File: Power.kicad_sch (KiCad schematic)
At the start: 26 parts, among them J8 USB_C_USB2.0_16P, Q1 Si2301CDS, Q2 Si2301CDS, U3 AMS1117-3.3, U4 TPS61230DRCR

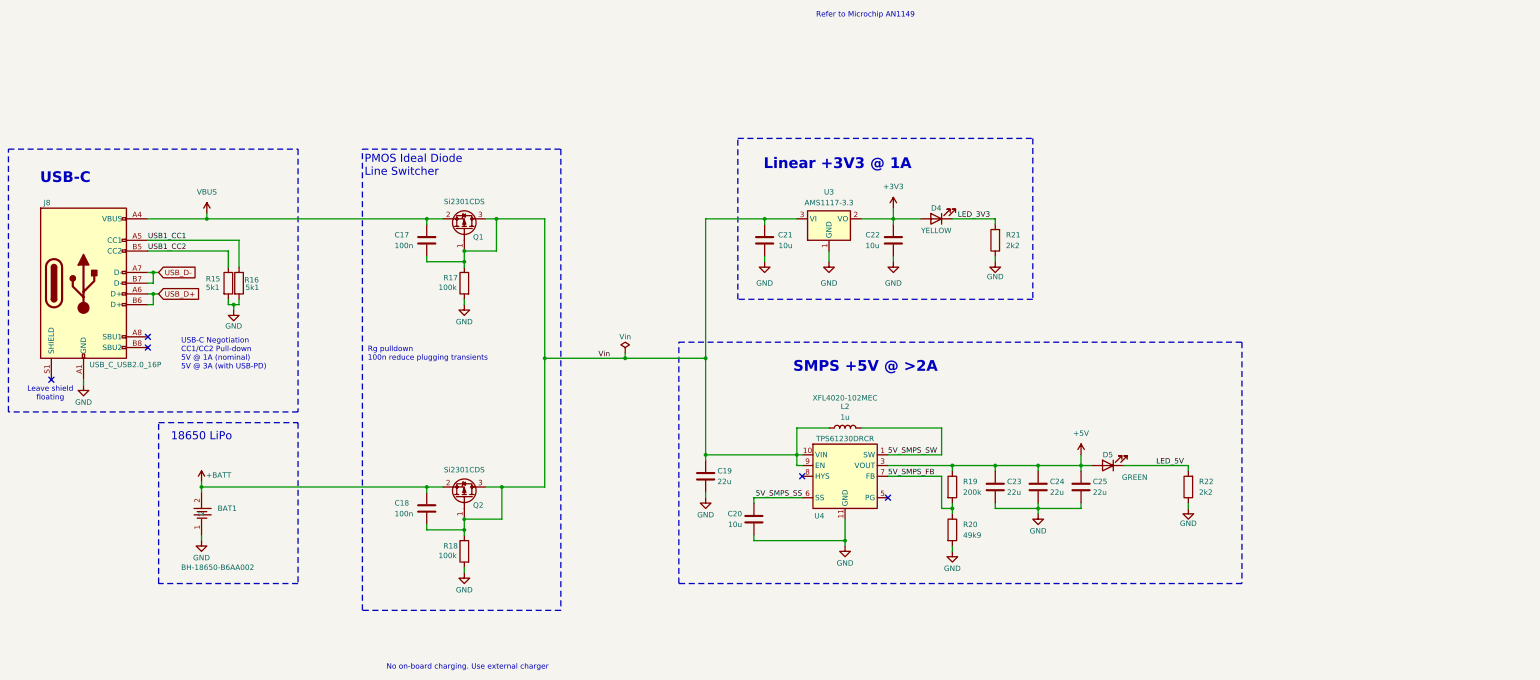
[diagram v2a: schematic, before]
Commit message: Add Buck-Boost 3V3 power
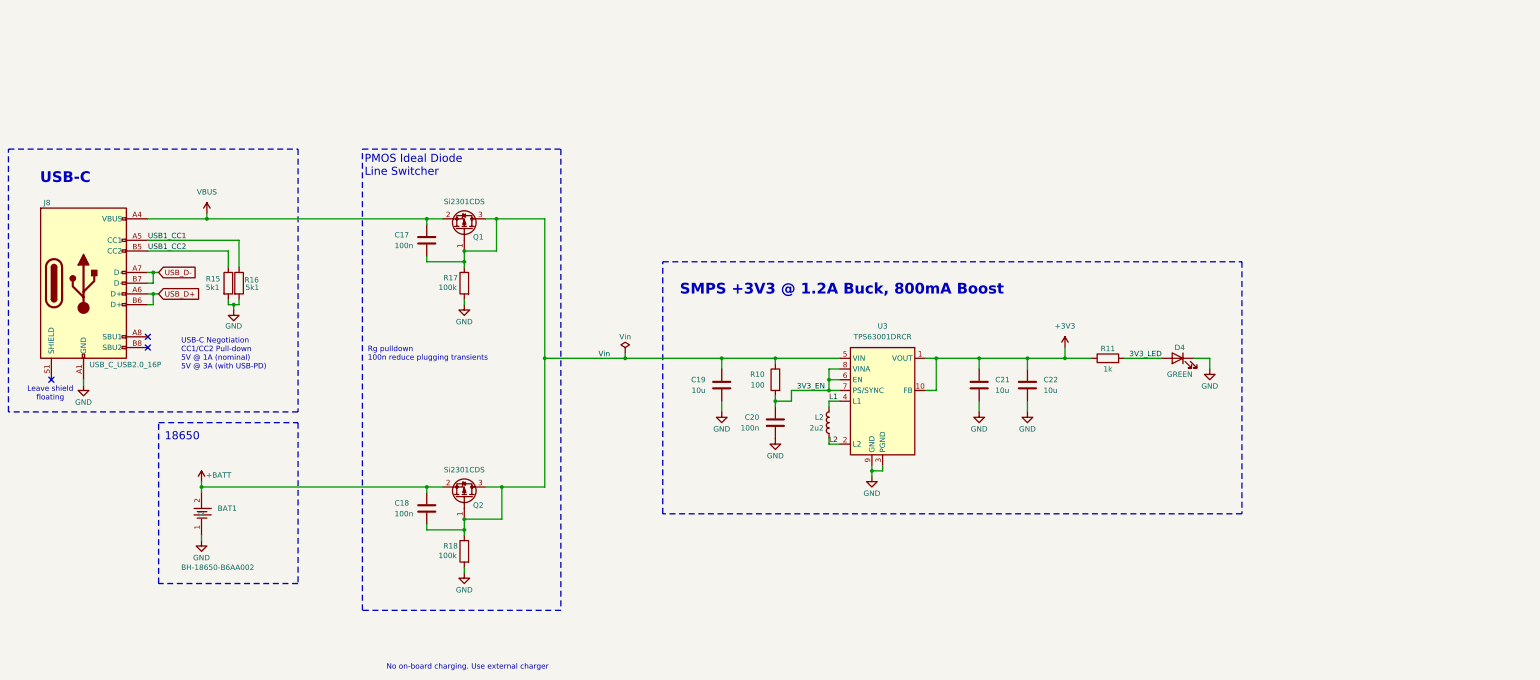
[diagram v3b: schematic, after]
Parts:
- removed C23, C24, C25: 22u, Capacitor_SMD:C_0805_2012Metric, symbol Device:C
- removed D5: GREEN, LED_SMD:LED_0603_1608Metric, symbol Device:LED
- removed R19: 200k, Resistor_SMD:R_0402_1005Metric, symbol Device:R
- removed R20: 49k9, Resistor_SMD:R_0402_1005Metric, symbol Device:R
- removed R21, R22: 2k2, Resistor_SMD:R_0603_1608Metric, symbol Device:R
- removed U3: AMS1117-3.3, Package_TO_SOT_SMD:SOT-223-3_TabPin2, symbol Regulator_Linear:AMS1117-3.3
- removed U4: TPS61230DRCR, Package_SON:Texas_S-PVSON-N10_ThermalVias, symbol Regulator_Switching:TPS61230DRC
- added R10: 100, Resistor_SMD:R_0402_1005Metric, symbol Device:R
- added R11: 1k, Resistor_SMD:R_0603_1608Metric, symbol Device:R
- added U3: TPS63001DRCR, Package_SON:Texas_DRC0010J_ThermalVias, symbol Regulator_Switching:TPS63001
- C19: value 22u -> 10u; footprint Capacitor_SMD:C_0805_2012Metric -> Capacitor_SMD:C_0603_1608Metric
- C20: value 10u -> 100n; footprint Capacitor_SMD:C_0603_1608Metric -> Capacitor_SMD:C_0402_1005Metric
- C21, C22: footprint Capacitor_SMD:C_0805_2012Metric -> Capacitor_SMD:C_0603_1608Metric
- D4: value YELLOW -> GREEN; footprint LED_SMD:LED_0603_1608Metric -> LED_SMD:LED_0805_2012Metric
- L2: value 1u -> 2u2; footprint easyeda2kicad:IND-SMD_L4.0-W4.0_XFL4020-102MEB -> easyeda2kicad:IND-SMD_L4.0-W4.0_VLS4012ET; LCSC Part C5355380 -> (none)
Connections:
- net LED_3V3 is gone; now on net GND: D4.1 (K)
- net +3V3: now also C21.1, R11.1, U3.1 (VOUT), U3.10 (FB); no longer D4.2 (A)
- net GND: now also U3.11 (PGND), U3.3 (PGND), U3.9 (GND)
- net Vin: now also R10.1, U3.5 (VIN); no longer C21.1, L2.1
- net 5V_SMPS_SS renamed 3V3_EN
- net 3V3_EN: now also R10.2, U3.6 (EN), U3.7 (PS/SYNC), U3.8 (VINA)
- net 5V_SMPS_SW renamed L2
- net L2: now also U3.2 (L2)
- new net 3V3_LED: D4.2 (A), R11.2
- new net L1: L2.1, U3.4 (L1)
- no-connect marks 5 -> 3
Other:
- note added: "18650"
- note added: "SMPS +3V3 @ 1.2A Buck, 800mA Boost"
- note removed: "18650 LiPo"
- note removed: "Linear +3V3 @ 1A"
- note removed: "Refer to Microchip AN1149"
- note removed: "SMPS +5V @ >2A"

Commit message: Added silkscreens label description and fixed DRC
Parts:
- U3: footprint Package_SON:Texas_DRC0010J_ThermalVias -> Package_SON:Texas_DRC0010J
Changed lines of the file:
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@@
 			)
 		)
-		(property "Footprint" "Package_SON:Texas_DRC0010J_ThermalVias"
+		(property "Footprint" "Package_SON:Texas_DRC0010J"
 			(at 261.62 120.65 0)
 			(effects

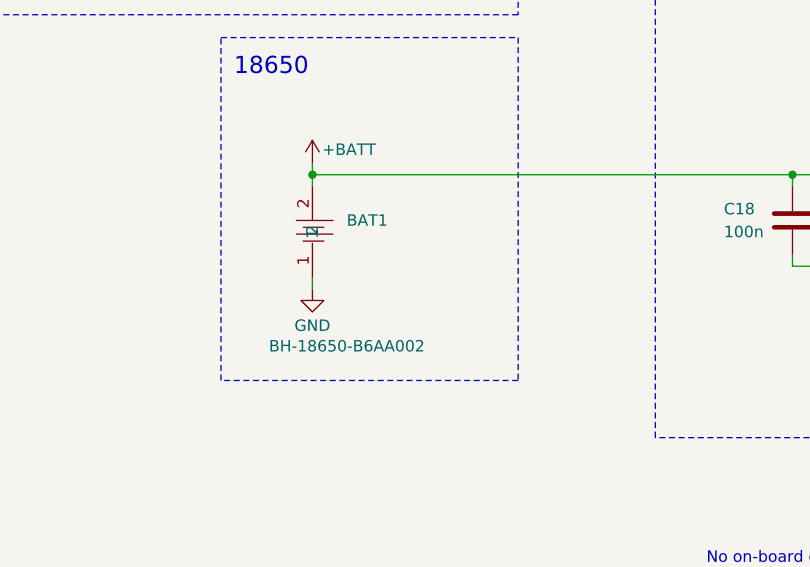
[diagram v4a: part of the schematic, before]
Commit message: Added 3D models and LCSC part numbers
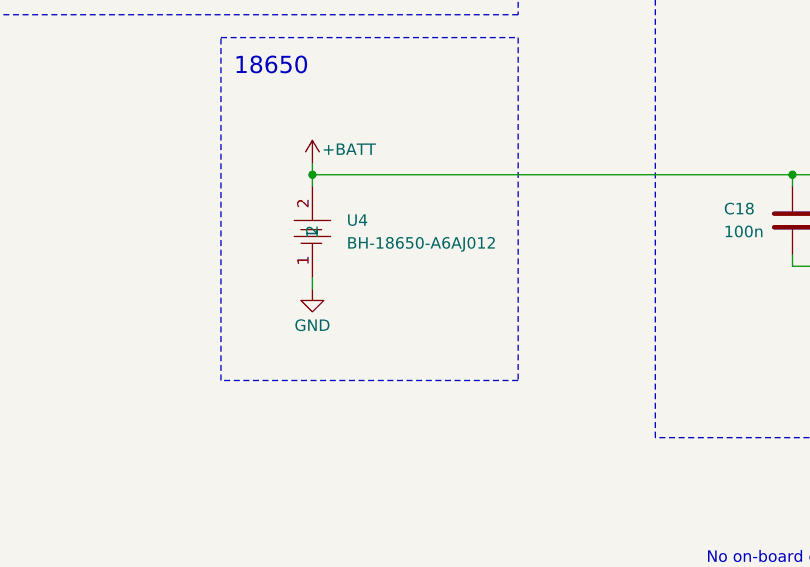
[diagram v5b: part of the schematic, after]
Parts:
- removed BAT1: BH-18650-B6AA002, easyeda2kicad:BATTERY-SMD_18650-1S-L77.1-W20.7-1, symbol easyeda2kicad:BH-18650-B6AA002
- added U4: BH-18650-A6AJ012, easyeda2kicad:BAT-TH_BH-18650-A6AJ012, symbol easyeda2kicad:BH-18650-A6AJ012
- J8: LCSC Part (none) -> C165948
- L2: LCSC Part (none) -> C76867
- Q1, Q2: LCSC Part (none) -> C10487
- U3: LCSC Part (none) -> C28060
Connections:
- net +BATT: now also U4.2
- net GND: now also U4.1

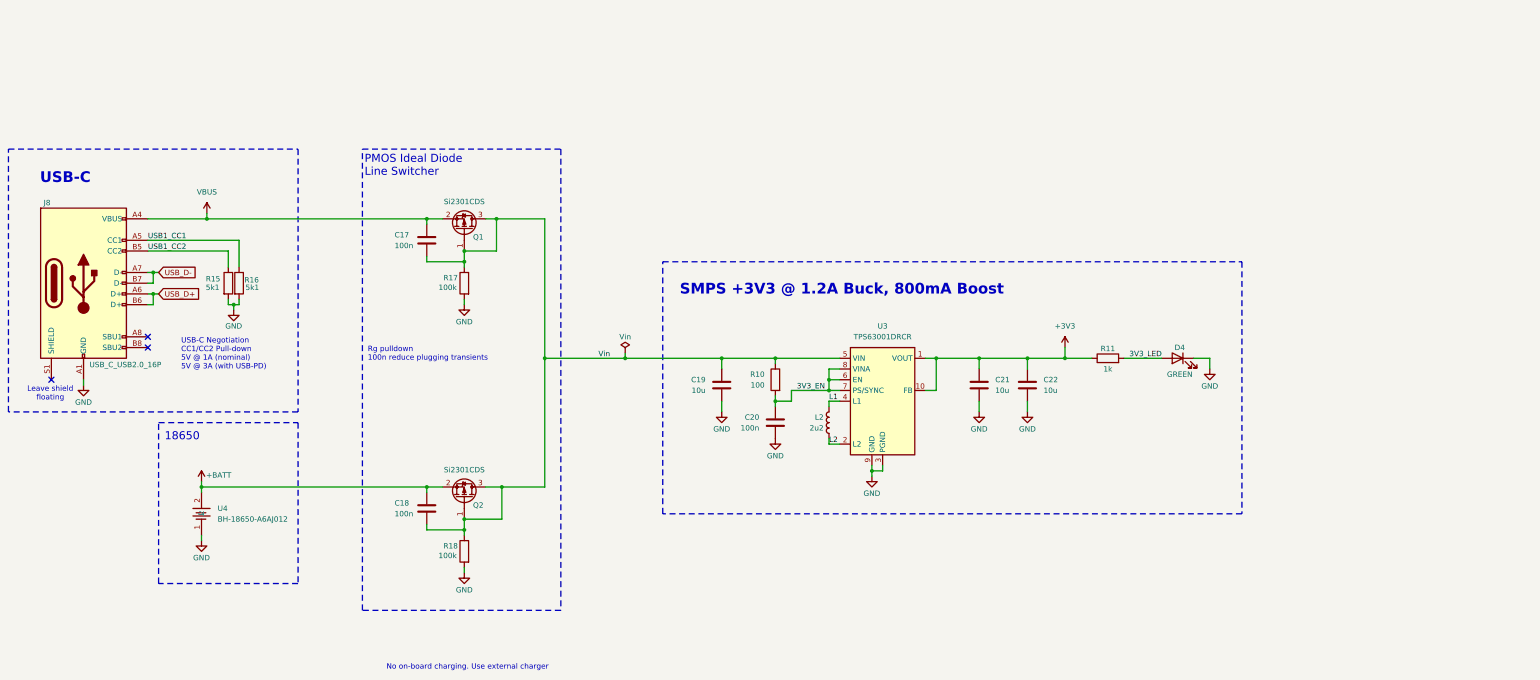
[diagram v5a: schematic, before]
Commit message: General DFM fixes
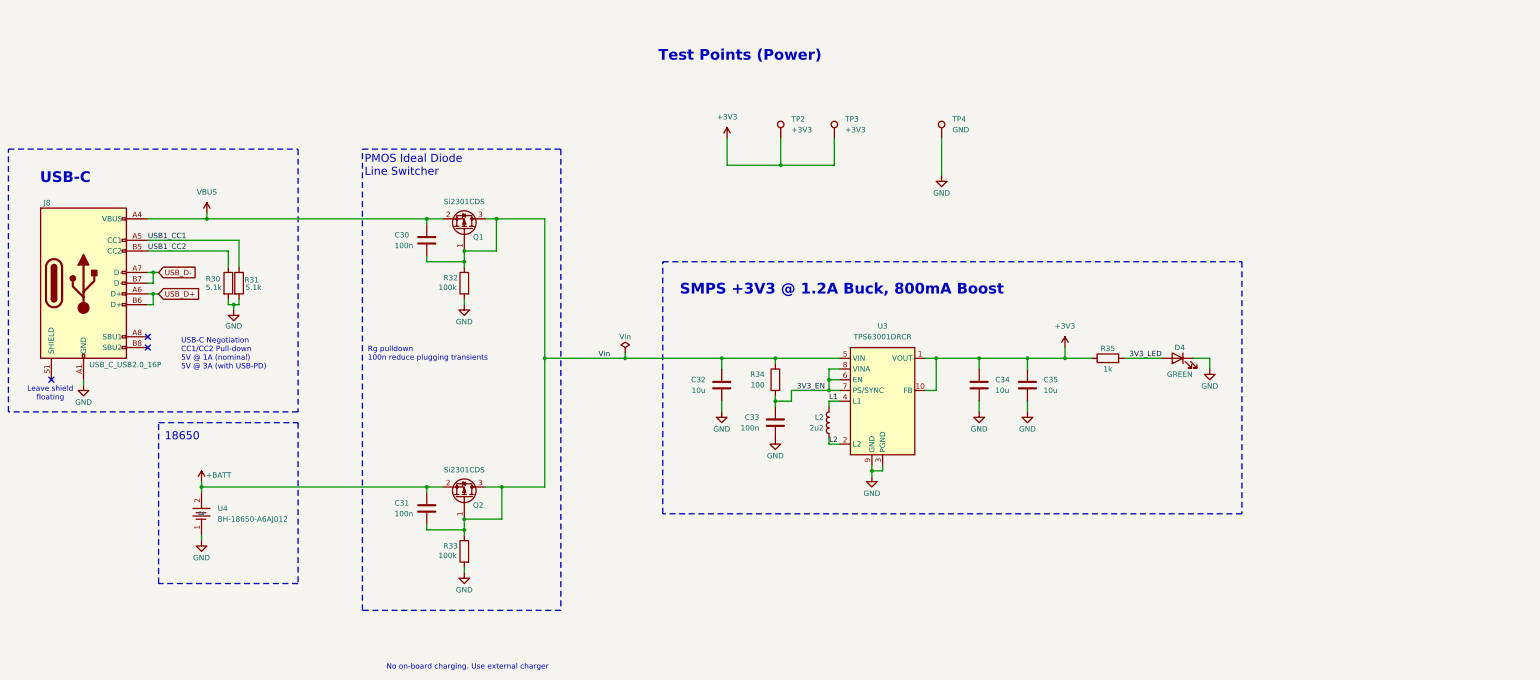
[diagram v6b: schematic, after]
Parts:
- added TP2, TP3: +3V3, TestPoint:TestPoint_Pad_D1.0mm, symbol Connector:TestPoint
- added TP4: GND, TestPoint:TestPoint_Pad_D1.0mm, symbol Connector:TestPoint
- C30: renamed from C17; LCSC Part (none) -> C1525
- C31: renamed from C18; LCSC Part (none) -> C1525
- C33: renamed from C20; LCSC Part (none) -> C1525
- R30: renamed from R15; value 5k1 -> 5.1k
- R31: renamed from R16; value 5k1 -> 5.1k
- renumbered C19 to C32, C21 to C34, C22 to C35, R17 to R32, R18 to R33, R10 to R34, R11 to R35
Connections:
- net +3V3: now also TP2.1, TP3.1
- net GND: now also TP4.1
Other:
- note added: "Test Points (Power)"

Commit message: BLV PCB v0.2
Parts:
- removed TP2: +3V3, TestPoint:TestPoint_Pad_D1.0mm, symbol Connector:TestPoint
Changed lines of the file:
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@@
 	)
 	(junction
-		(at 215.9 50.8)
-		(diameter 0)
-		(color 0 0 0 0)
-	)
-	(junction
 		(at 252.73 96.52)
 		(diameter 0)
@@
 	(wire
 		(pts
-			(xy 228.6 50.8) (xy 215.9 50.8)
+			(xy 203.2 50.8) (xy 228.6 50.8)
 		)
 		(stroke
@@
 	(wire
 		(pts
-			(xy 215.9 50.8) (xy 203.2 50.8)
-		)
-		(stroke
-			(width 0)
-			(type default)
-		)
-	)
-	(wire
-		(pts
 			(xy 68.58 76.2) (xy 67.31 76.2)
 		)
@@
 	(wire
 		(pts
-			(xy 215.9 44.45) (xy 215.9 50.8)
-		)
-		(stroke
-			(width 0)
-			(type default)
-		)
-	)
-	(wire
-		(pts
 			(xy 262.89 96.52) (xy 262.89 99.06)
 		)
@@
 					(unit 1)
 				)
-			)
-		)
-	)
-	(symbol
-		(lib_id "Connector:TestPoint")
-		(at 215.9 44.45 0)
-		(unit 1)
-		(exclude_from_sim no)
-		(in_bom yes)
-		(on_board yes)
-		(dnp no)
-		(fields_autoplaced yes)
-		(property "Reference" "TP2"
-			(at 218.44 39.8779 0)
-			(effects
-				(font
-					(size 1.27 1.27)
-				)
-				(justify left)
-			)
-		)
-		(property "Value" "+3V3"
-			(at 218.44 42.4179 0)
-			(effects
-				(font
-					(size 1.27 1.27)
-				)
-				(justify left)
-			)
-		)
-		(property "Footprint" "TestPoint:TestPoint_Pad_D1.0mm"
-			(at 220.98 44.45 0)
-			(effects
-				(font
-					(size 1.27 1.27)
-				)
-				(hide yes)
-			)
-		)
-		(property "Datasheet" "~"
-			(at 220.98 44.45 0)
-			(effects
-				(font
-					(size 1.27 1.27)
-				)
-				(hide yes)
-			)
-		)
-		(property "Description" "test point"
-			(at 215.9 44.45 0)
-			(effects
-				(font
-					(size 1.27 1.27)
-				)
-				(hide yes)
-			)
-		)
-		(pin "1"
-		)
-		(instances
-			(project ""
-				(path "/e98ed281-6a46-49b2-ab41-e3d95fdf6973/2ac26712-adbd-4e92-84f1-3c660d93b184"
-					(reference "TP2")
-					(unit 1)
-				)
